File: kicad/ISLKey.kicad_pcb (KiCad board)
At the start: 2 copper layers, 148.3 x 127.5 mm, 46 parts, among them J10 5-60V AC/DC IN, J11 12V OUT (lock/aux), J13 TTGO batt pads, J3 Exit btn, J4 Door contact, J5 Tamper, J6 LOCK COM/NO/NC, J7 AUX COM/NO/NC, J8 Fire volt-free, J9 Fire link COM-Fire, K1 SRD-05VDC-SL-C, K2 SRD-05VDC-SL-C, M1 TTGO T-Display, Q1 PN2222A, Q2 PN2222A, U1 PC817, U3 TEN20-2412WIN, U4 TSR-1-2450, U5 DS3231M

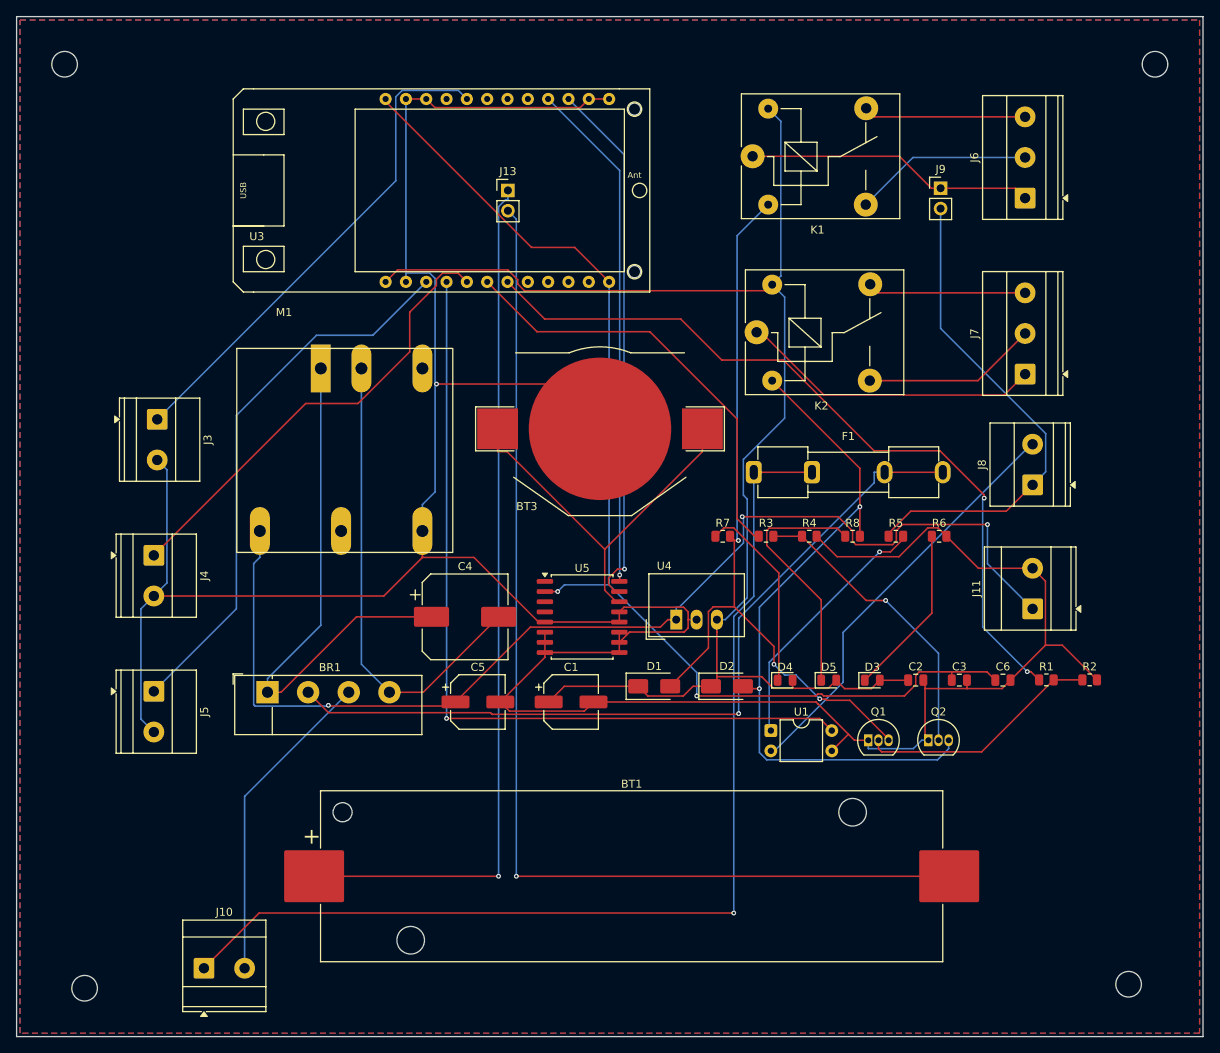
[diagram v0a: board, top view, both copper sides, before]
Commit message: kicad: swap isolated DC-DC to Traco TMR10-2412WIR (was TEN20, too big)
TEN20-2412WIN (25.4x25.4mm 20W 1"x1" brick) -> TMR10-2412WIR (13.7x23.6mm,
10W, 9-36V->isolated 12V) -- ~half the area, powers logic + a ~6W lock.
Rewired U3 (1=-Vin/PGND, 2=+Vin/RAWP, 3=Remote NC=on, 6=+Vout/12V,
7=-Vout/GND, 9/10=Case NC). Footprint swapped in place on the hand-placed
board, re-routed (GND-as-traces): 328 traces + 25 vias, DRC clean bar
cosmetic silk text-height.

Co-Authored-By: Claude Opus 4.8 <noreply@anthropic.com>
Claude-Session: https://claude.ai/code/session_01WaJbCVpNNC7xF4fkqWpjpA
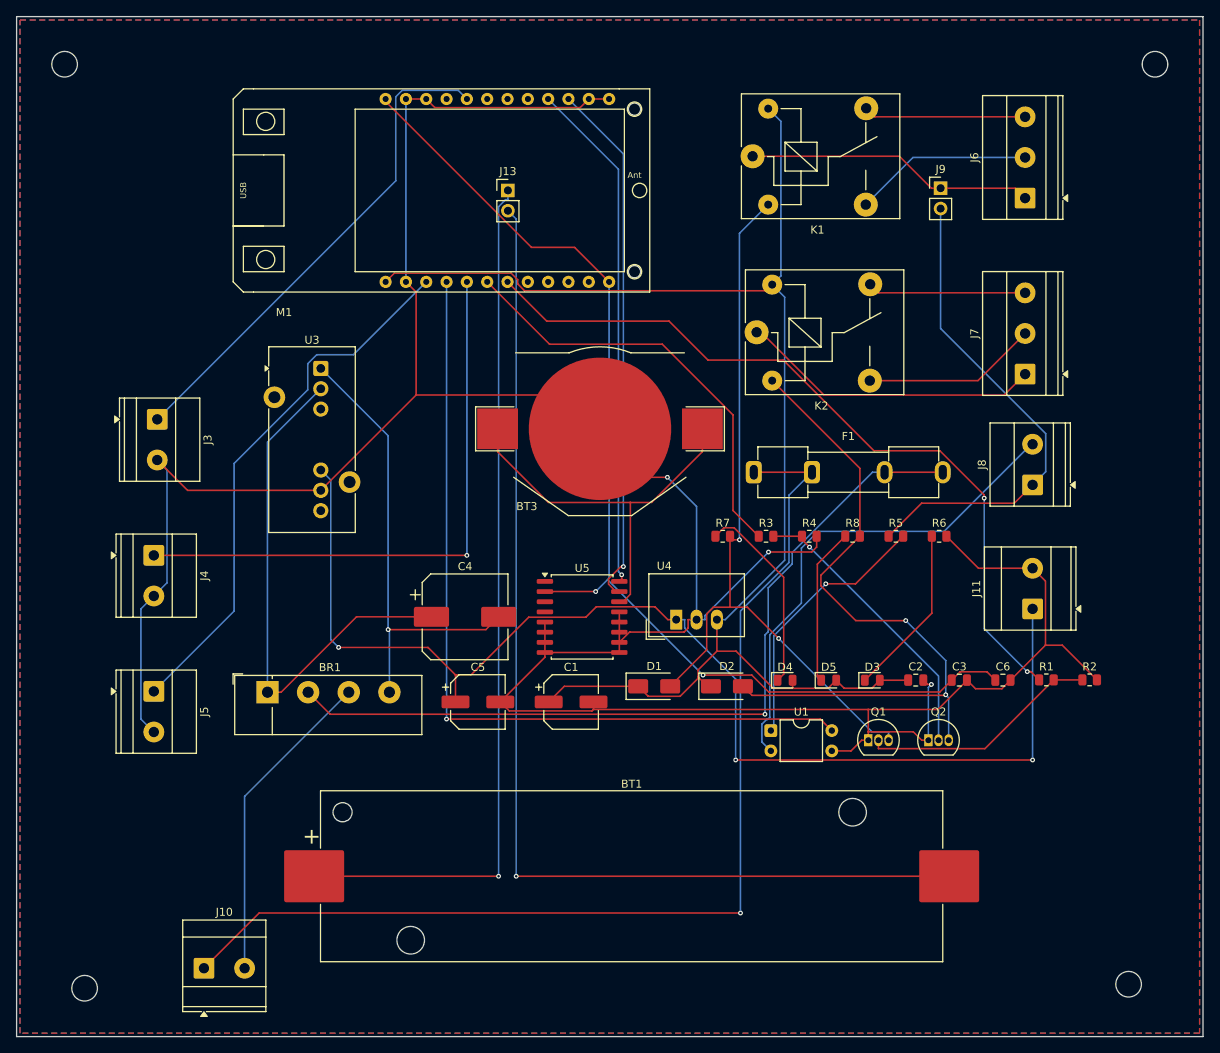
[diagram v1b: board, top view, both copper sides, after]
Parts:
- U3: value TEN20-2412WIN -> TMR10-2412WIR; footprint TEN20_TRACO -> Converter_DCDC_TRACO_TMR10-24xxWIR_48xxWIR_72xxWIR_THT
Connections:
- U3 pad 1: RAWP -> PGND
- U3 pad 2: PGND -> RAWP
- U3 pad 3: +12V -> (no net)
- U3 pad 6: (no net) -> +12V
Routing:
- net DOOR: track 57.6 -> 73.3 mm, vias 0 -> 1
- net D5K: track 31.9 -> 19.6 mm
- net GND: track 394.6 -> 382.8 mm, vias 1 -> 3
- net FIRE_B: track 52.2 -> 62.2 mm
- net +12V: track 143.6 -> 151.5 mm
- net +3V3: track 143.2 -> 139.1 mm
- net ACL: track 132.5 -> 136.0 mm
- net RAWP: track 67.6 -> 65.1 mm
- net ACIN1: track 100.8 -> 102.8 mm
- net TAMPER: track 69.4 -> 68.0 mm
- net RLY2_B: track 37.6 -> 36.2 mm
- net OPTO_A: track 32.1 -> 33.3 mm
- net +5V: track 178.3 -> 179.5 mm
- net PGND: track 59.5 -> 58.5 mm, vias 0 -> 1
- net RTC_VBAT: track 49.0 -> 49.8 mm
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
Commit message: kicad: add TMR10 Ctrl/Remote enable jumper (J15)
2-pin jumper J15 links U3 pin3 (Ctrl/Remote, net DCDC_CTRL) to +Vin (RAWP):
fit the shunt to tie Ctrl->+Vin (forces ON regardless of the module's logic
polarity); leave open = ON for positive-logic parts. Placed in the space
freed by the smaller TMR10; re-routed (356 traces + 26 vias, DRC clean bar
cosmetic silk).

Co-Authored-By: Claude Opus 4.8 <noreply@anthropic.com>
Claude-Session: https://claude.ai/code/session_01WaJbCVpNNC7xF4fkqWpjpA
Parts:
- added J15: DCDC ON, PinHeader_1x02_P2.54mm_Vertical, F.Cu at (130.5, 69.4)
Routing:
- net GND: track 382.8 -> 407.6 mm, vias 3 -> 0
- net RAWP: track 65.1 -> 78.1 mm
- net FIRE_B: track 62.2 -> 52.0 mm
- net +12V: track 151.5 -> 142.2 mm, vias 3 -> 5
- net ACIN1: track 102.8 -> 110.1 mm, vias 1 -> 2
- net RLY2_B: track 36.2 -> 43.1 mm
- net +5V: track 179.5 -> 174.8 mm, vias 0 -> 1
- net FIRE_SENSE: track 103.4 -> 100.0 mm
- net PGND: track 58.5 -> 61.6 mm, vias 1 -> 0
- net D4K: track 24.7 -> 22.2 mm, vias 0 -> 2
- net OPTO_A: track 33.3 -> 31.1 mm
- net ACL: track 136.0 -> 134.0 mm
- net +3V3: track 139.1 -> 141.0 mm
- net K2_C: track 87.6 -> 85.8 mm, vias 2 -> 1
- net D3K: track 21.5 -> 22.7 mm
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
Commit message: kicad: fix U3/F1 3D models + add functional silk labels
- 3D: TMR10 and Keystone-3512 fuse-holder .step models aren't in this KiCad
  3D package (referenced files absent). Repointed U3 -> generic
  Converter_DCDC_TRACO_TMR-xxxx and F1 -> Fuseholder_Cylinder-5x20mm_Schurter
  (both exist) so they render (approximate stand-ins).
- Silk: added functional labels on F.SilkS at each terminal/jumper
  (EXIT/DOOR/TAMPER/LOCK/AUX/FIRE/5-60V IN/12V OUT/FIRE LINK/DCDC ON/BATT)
  and hid the Jxx refdes on those parts. Remaining silk_overlap DRC is
  cosmetic (silk-to-silk on a dense board).

Co-Authored-By: Claude Opus 4.8 <noreply@anthropic.com>
Claude-Session: https://claude.ai/code/session_01WaJbCVpNNC7xF4fkqWpjpA
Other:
- board text added: "12V OUT"
- board text added: "5-60V IN"
- board text added: "AUX"
- board text added: "BATT"
- board text added: "DCDC ON"
- board text added: "DOOR"
- board text added: "EXIT"
- board text added: "FIRE"
- board text added: "FIRE LINK"
- board text added: "LOCK"
- board text added: "TAMPER"
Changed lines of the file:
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@@
 			(at 2.54 -7.02 0)
 			(layer "F.SilkS")
+			(hide yes)
 			(effects
 				(font
@@
 			(at 5.08 -6.32 90)
 			(layer "F.SilkS")
+			(hide yes)
 			(effects
 				(font
@@
 		)
 		(embedded_fonts no)
-		(model "${KICAD10_3DMODEL_DIR}/Fuse.3dshapes/Fuseholder_Clip-5x20mm_Keystone_3512_Inline_P23.62x7.27mm_D1.02x1.57mm_Horizontal.step"
+		(model "${KICAD10_3DMODEL_DIR}/Fuse.3dshapes/Fuseholder_Cylinder-5x20mm_Schurter_0031_8201_Horizontal_Open.step"
 			(offset
 				(xyz 0 0 0)
@@
 			(at 2.54 -6.32 90)
 			(layer "F.SilkS")
+			(hide yes)
 			(effects
 				(font
@@
 			(at 2.54 -6.32 90)
 			(layer "F.SilkS")
+			(hide yes)
 			(effects
 				(font
@@
 			(at 2.54 -6.32 90)
 			(layer "F.SilkS")
+			(hide yes)
 			(effects
 				(font
@@
 			(at 0 -2.38 0)
 			(layer "F.SilkS")
+			(hide yes)
 			(effects
 				(font
@@
 			(at 5.08 -6.32 90)
 			(layer "F.SilkS")
+			(hide yes)
 			(effects
 				(font
@@
 			(at 0 -2.38 0)
 			(layer "F.SilkS")
+			(hide yes)
 			(effects
 				(font
@@
 			(at 0 -2.38 0)
 			(layer "F.SilkS")
+			(hide yes)
 			(effects
 				(font
@@
 			(at 2.54 -7.02 90)
 			(layer "F.SilkS")
+			(hide yes)
 			(effects
 				(font
@@
 		)
 		(embedded_fonts no)
-		(model "${KICAD10_3DMODEL_DIR}/Converter_DCDC.3dshapes/Converter_DCDC_TRACO_TMR10-24xxWIR_48xxWIR_72xxWIR_THT.step"
+		(model "${KICAD10_3DMODEL_DIR}/Converter_DCDC.3dshapes/Converter_DCDC_TRACO_TMR-xxxx_THT.step"
 			(offset
 				(xyz 0 0 0)
@@
 			(at 2.54 -6.32 90)
 			(layer "F.SilkS")
+			(hide yes)
 			(effects
 				(font
@@
 		(layer "Edge.Cuts")
 	)
+	(gr_text "TAMPER"
+		(at 100.887172 108.215714 0)
+		(layer "F.SilkS")
+		(effects
+			(font
+				(size 1 1)
+				(thickness 0.15)
+			)
+		)
+	)
+	(gr_text "DOOR"
+		(at 101.146074 92.461722 0)
+		(layer "F.SilkS")
+		(effects
+			(font
+				(size 1 1)
+				(thickness 0.15)
+			)
+		)
+	)
+	(gr_text "EXIT"
+		(at 101.458742 76.7826 0)
+		(layer "F.SilkS")
+		(effects
+			(font
+				(size 1 1)
+				(thickness 0.15)
+			)
+		)
+	)
+	(gr_text "5-60V IN"
+		(at 105.964848 141.041558 0)
+		(layer "F.SilkS")
+		(effects
+			(font
+				(size 1 1)
+				(thickness 0.15)
+			)
+		)
+	)
+	(gr_text "DCDC ON"
+		(at 133.94541 72.304173 0)
+		(layer "F.SilkS")
+		(effects
+			(font
+				(size 1 1)
+				(thickness 0.15)
+			)
+		)
+	)
+	(gr_text "BATT"
+		(at 142.219102 51.436528 0)
+		(layer "F.SilkS")
+		(effects
+			(font
+				(size 1 1)
+				(thickness 0.15)
+			)
+		)
+	)
+	(gr_text "FIRE LINK"
+		(at 191.854169 50.072724 0)
+		(layer "F.SilkS")
+		(effects
+			(font
+				(size 1 1)
+				(thickness 0.15)
+			)
+		)
+	)
+	(gr_text "AUX"
+		(at 201.340701 71.640903 0)
+		(layer "F.SilkS")
+		(effects
+			(font
+				(size 1 1)
+				(thickness 0.15)
+			)
+		)
+	)
+	(gr_text "FIRE"
+		(at 202.021749 84.376893 0)
+		(layer "F.SilkS")
+		(effects
+			(font
+				(size 1 1)
+				(thickness 0.15)
+			)
+		)
+	)
+	(gr_text "LOCK"
+		(at 202.035491 50.881517 0)
+		(layer "F.SilkS")
+		(effects
+			(font
+				(size 1 1)
+				(thickness 0.15)
+			)
+		)
+	)
+	(gr_text "12V OUT"
+		(at 202.082865 98.575393 0)
+		(layer "F.SilkS")
+		(effects
+			(font
+				(size 1 1)
+				(thickness 0.15)
+			)
+		)
+	)
 	(segment

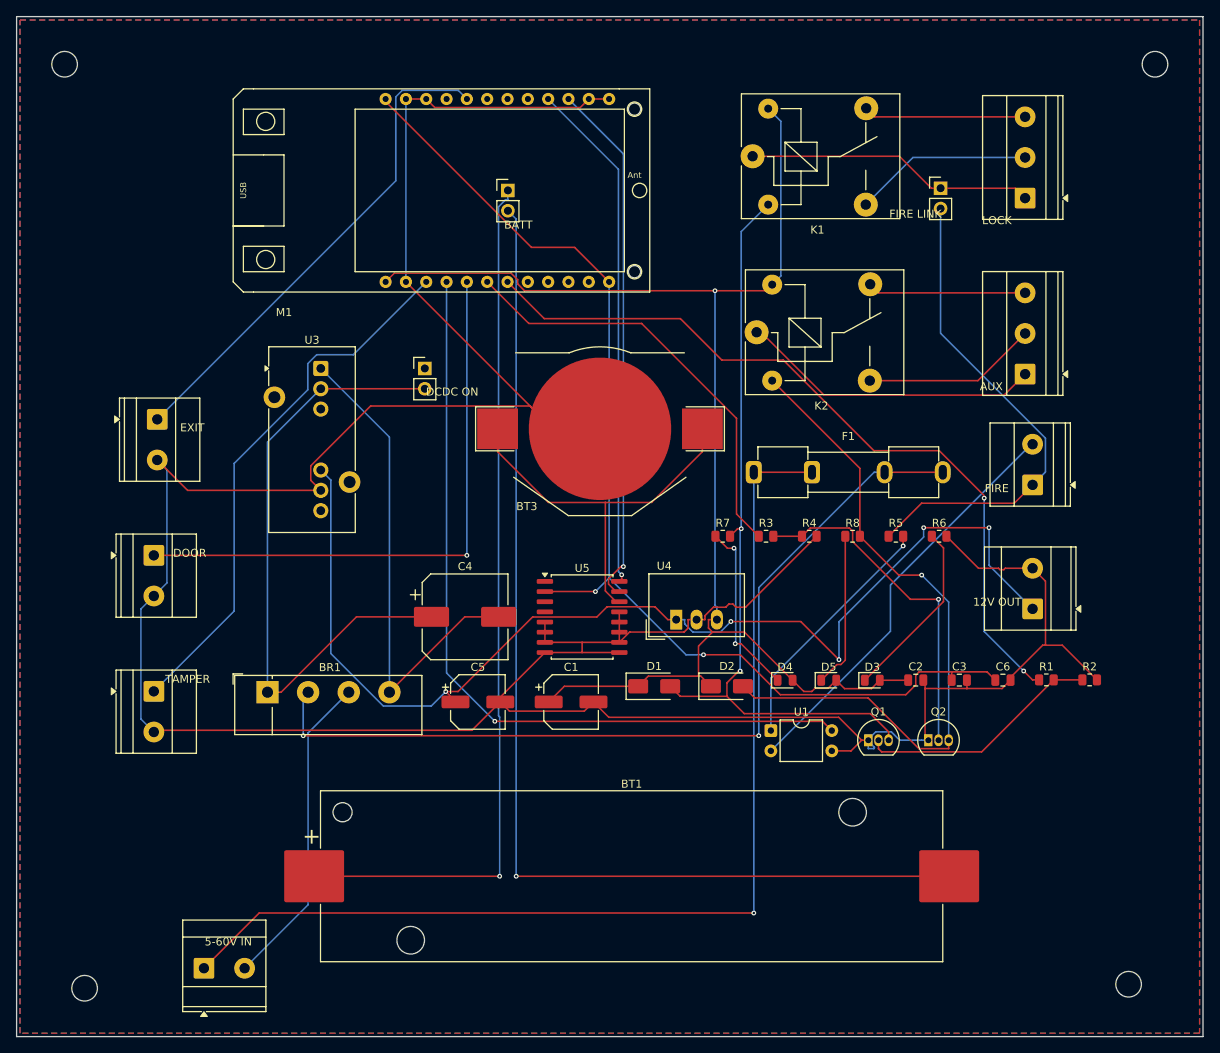
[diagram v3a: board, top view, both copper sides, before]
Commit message: kicad: fix broken DCDC_CTRL jumper net + re-route
The U3->TMR10 swap never assigned U3 pin3, so the DCDC_CTRL net didn't exist
and J15 (the enable jumper) connected to nothing. Re-synced all pad nets from
the schematic manifest (only U3.3/J15.1 differed) and re-routed: 346 traces +
23 vias, 0 unconnected. User's silk edits preserved. DRC = cosmetic only.

Co-Authored-By: Claude Opus 4.8 <noreply@anthropic.com>
Claude-Session: https://claude.ai/code/session_01WaJbCVpNNC7xF4fkqWpjpA
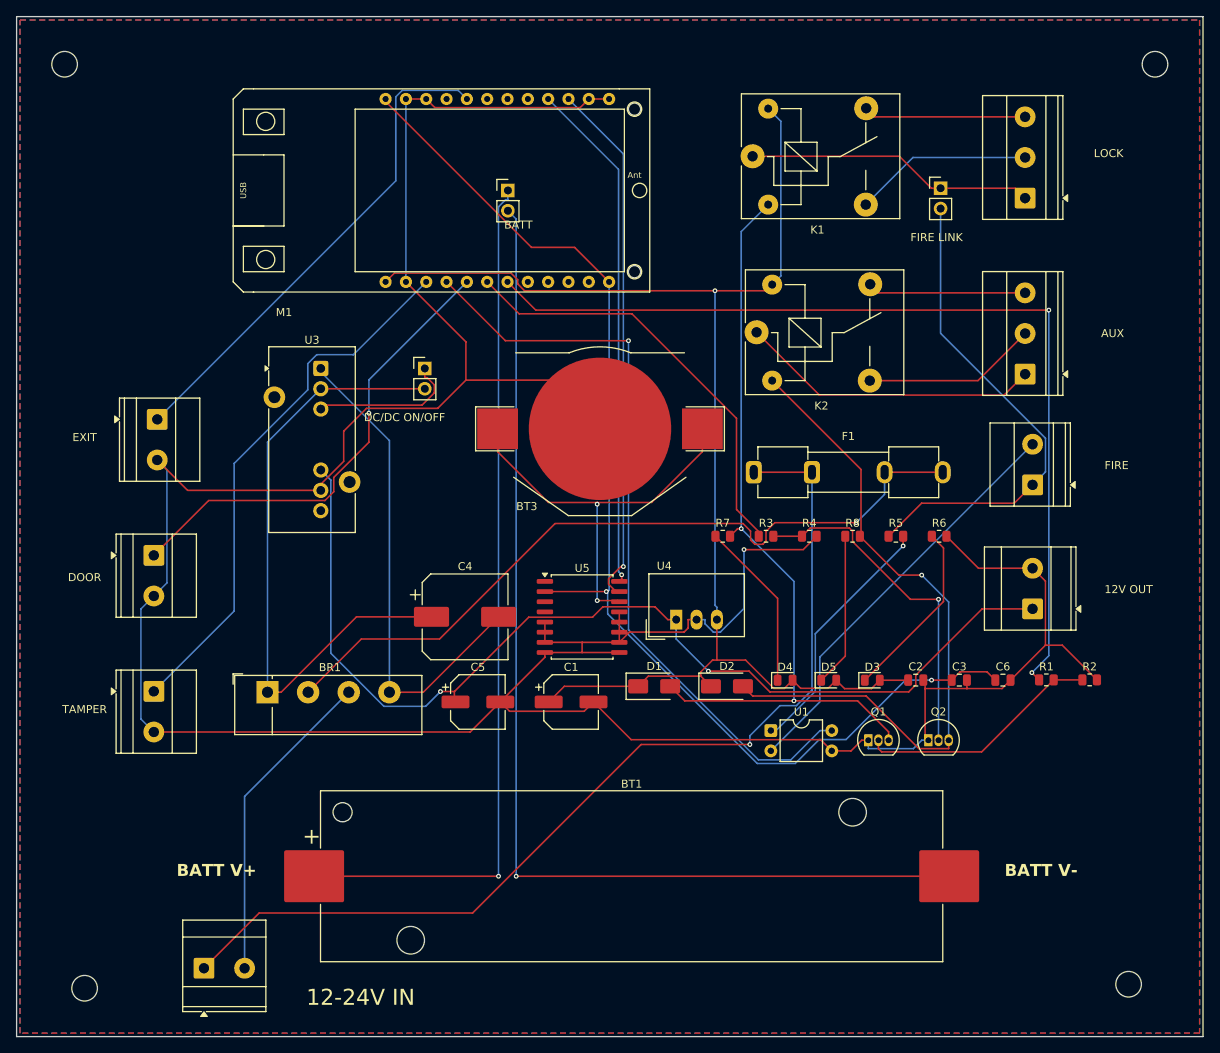
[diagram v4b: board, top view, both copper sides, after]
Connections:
- J15 pad 1: (no net) -> DCDC_CTRL
- U3 pad 3: (no net) -> DCDC_CTRL
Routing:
- net RLY1: track 97.0 -> 116.6 mm
- net DCDC_CTRL: track 0.00 -> 18.7 mm
- net DOOR: track 73.3 -> 58.9 mm
- net ACIN1: track 110.1 -> 95.8 mm, vias 2 -> 1
- net +12V: track 142.2 -> 131.2 mm, vias 5 -> 2
- net ACL: track 134.0 -> 125.5 mm
- net +3V3: track 141.0 -> 148.4 mm
- net GND: track 407.6 -> 401.5 mm, vias 0 -> 1
- net FIRE_SENSE: track 100.0 -> 95.6 mm
- net K1_C: track 96.2 -> 98.7 mm
- net +5V: track 174.8 -> 172.5 mm
- net RTC_VBAT: track 49.9 -> 51.7 mm, vias 0 -> 2
- net D4K: track 22.2 -> 21.2 mm, vias 2 -> 0
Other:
- board text added: "12-24V IN"
- board text added: "BATT V+"
- board text added: "BATT V-"
- board text added: "DC/DC ON/OFF"
- board text removed: "5-60V IN"
- board text removed: "DCDC ON"
